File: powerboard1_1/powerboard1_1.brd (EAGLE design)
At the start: 149.9 x 86.4 mm, 103 parts, among them Q1 IPP80P03P4L04AKSA1, U1 UWQ-12/20-T48NBS-C, U2 UWE-5/20-Q48NB-C, U3 UWE-3.3/30-Q48NB-C

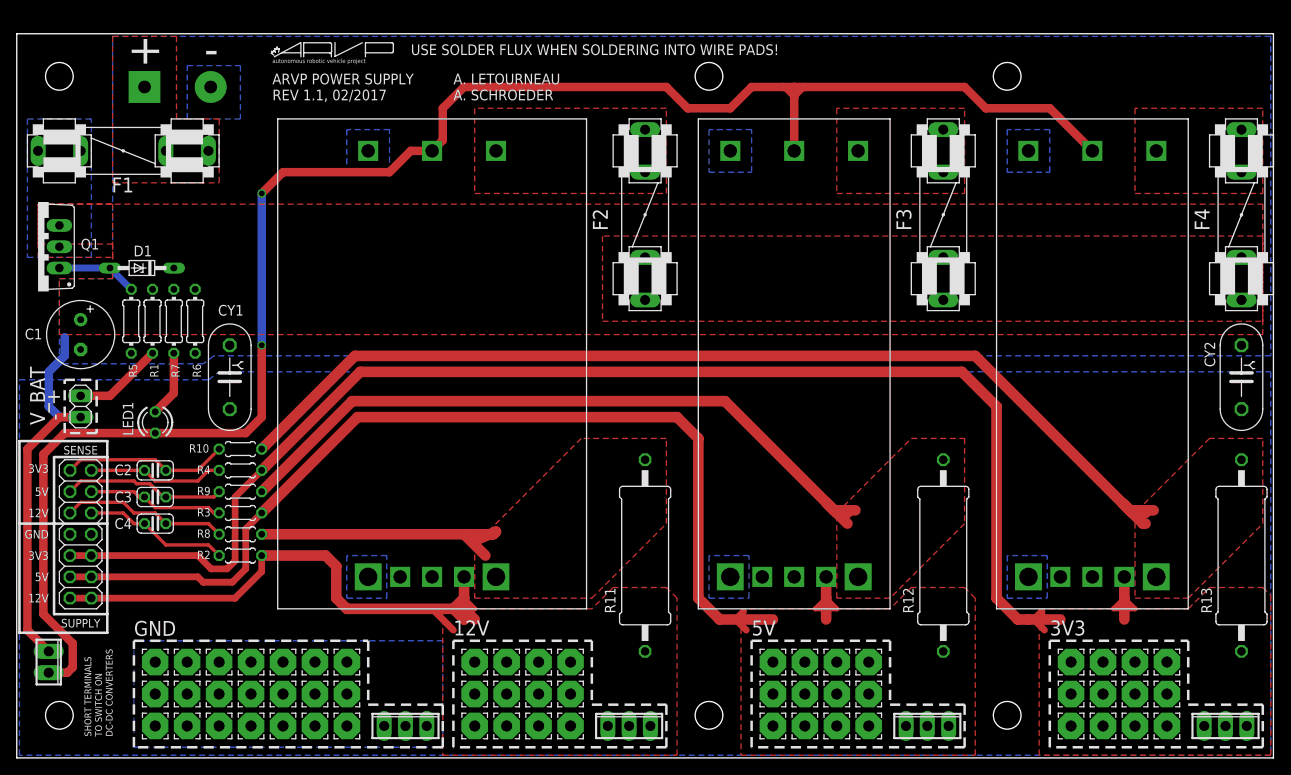
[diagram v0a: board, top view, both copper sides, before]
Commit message: Modified more traces and polygons; Fixed power board library
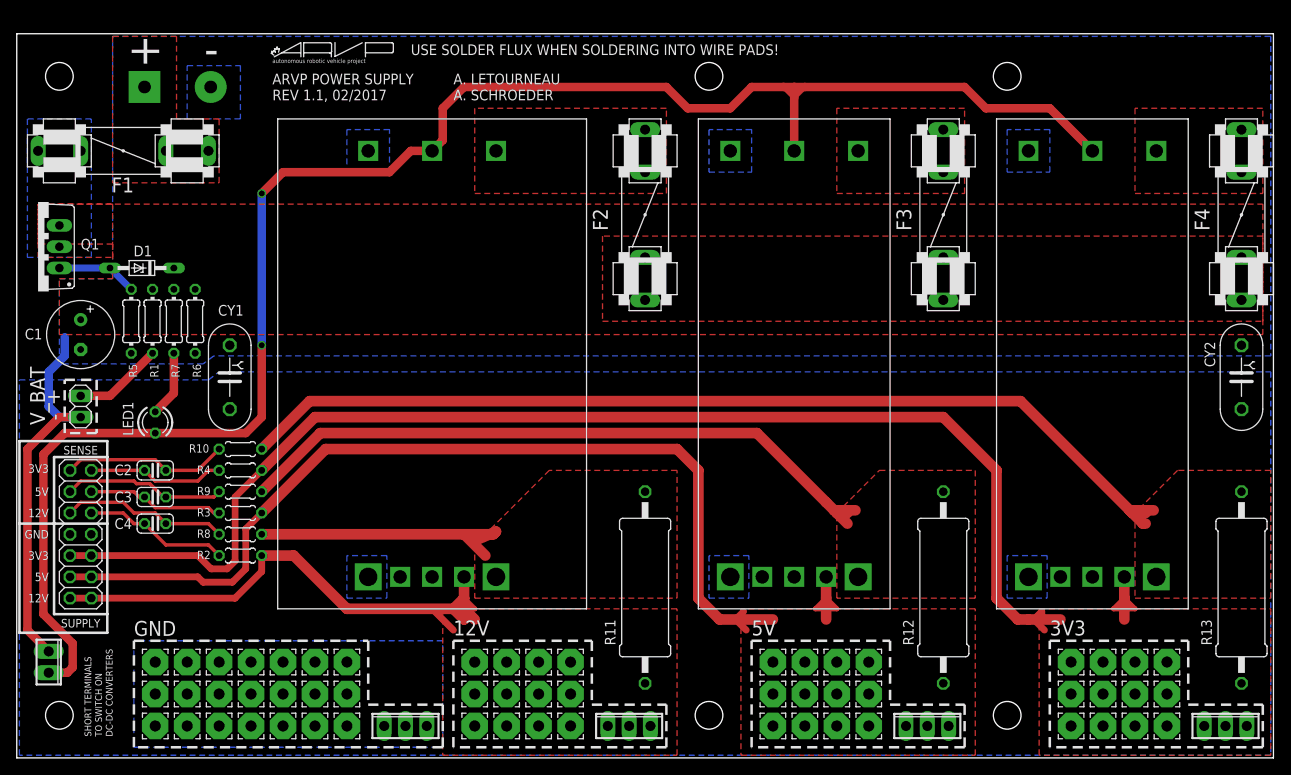
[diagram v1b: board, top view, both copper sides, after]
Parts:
- U4: value UWQ-12/20-T48NBS-C -> UWQ-12/20-T48NTB-C
- moved R11 3.81 mm to (104.1, 11.4)
- moved R12 3.81 mm to (139.7, 11.4)
- moved R13 3.81 mm to (175.3, 11.4)
- renumbered U1 to U4
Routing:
- net 3V3-SENSE: track 174.7 -> 165.7 mm
- net 3V3+SENSE: track 125.4 -> 118.3 mm
- net 5V+SENSE: track 87.3 -> 81.0 mm
- net 5V-SENSE: track 131.2 -> 125.8 mm
- net 12V-SENSE: track 73.5 -> 71.2 mm

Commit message: Replaced output rail terminals with filtering capacitors; Modified LED circuit; Modified traces and polygons
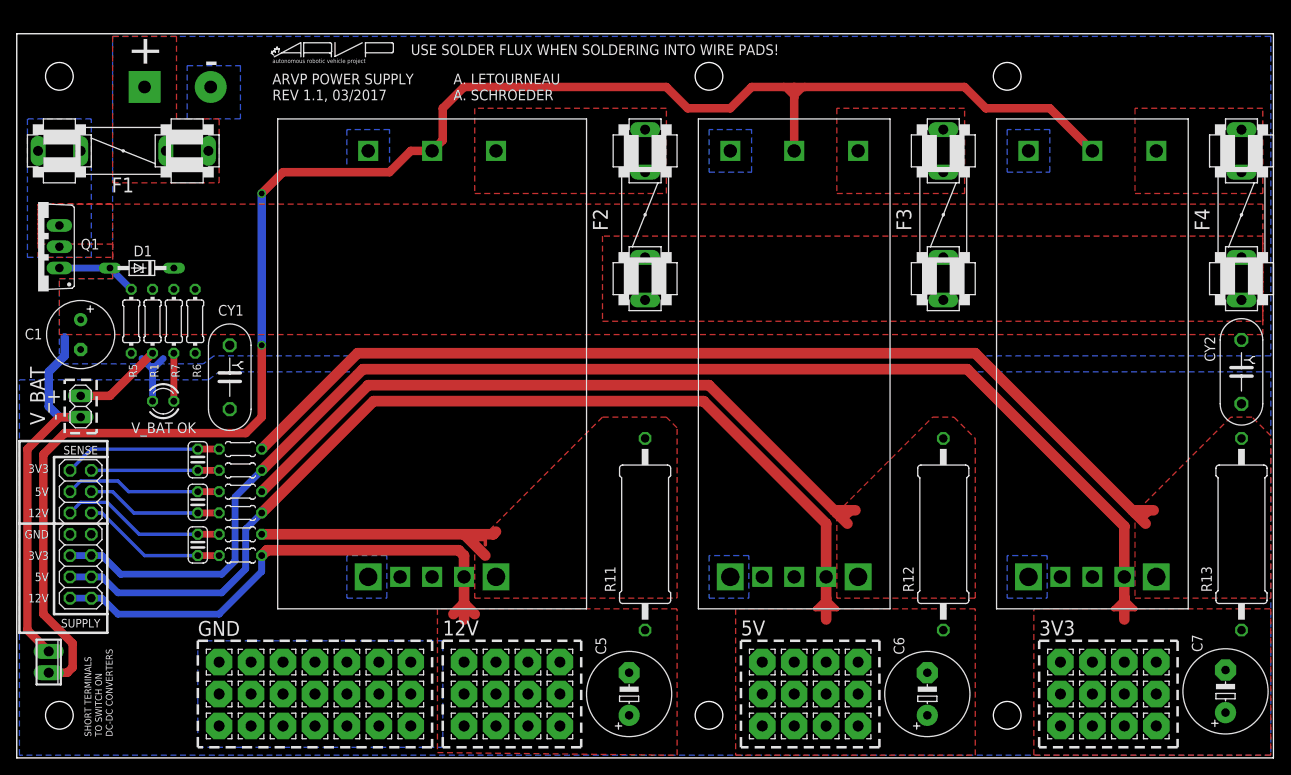
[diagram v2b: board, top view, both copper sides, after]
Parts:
- removed X2, X3, X4, X5: (no value), con-phoenix-254:3POL254
- added C5, C6, C7: (no value), rcl:E5-10,5
- moved PAD12 7.62 mm to (53.3, -1.27)
- moved PAD13 7.62 mm to (76.2, -5.08)
- moved PAD14 7.62 mm to (72.4, -5.08)
- moved PAD19 7.62 mm to (53.3, 2.54)
- moved PAD20 7.62 mm to (76.2, -1.27)
- moved PAD21 7.62 mm to (72.4, -1.27)
- moved PAD5 7.62 mm to (72.4, 2.54)
- moved PAD6 7.62 mm to (76.2, 2.54)
- moved PAD7 7.62 mm to (53.3, -5.08)
- moved PAD1 7.62 mm to (57.1, 2.54)
- moved PAD10 7.62 mm to (64.8, -1.27)
- moved PAD11 7.62 mm to (68.6, -1.27)
- moved PAD15 7.62 mm to (68.6, -5.08)
- moved PAD16 7.62 mm to (64.8, -5.08)
- moved PAD17 7.62 mm to (61.0, -5.08)
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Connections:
- net 12V-SENSE: now also C5.+; no longer X2.1, X2.2, X2.3
- net 3V3-SENSE: now also C7.+; no longer X5.1, X5.2, X5.3
- net 5V-SENSE: now also C6.+; no longer X4.1, X4.2, X4.3
- net GND: now also C5.-, C6.-, C7.-; no longer X3.1, X3.2, X3.3
- net ON/OFF: no longer LED1.K
- net V-: now also LED1.K
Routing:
- net V-: track 46.5 -> 54.2 mm
- net 12V-SENSE: track 71.2 -> 63.5 mm
- net 5V+SENSE: track 81.0 -> 85.8 mm
- net 3V3+SENSE: track 118.3 -> 122.4 mm
- net N$1: track 7.91 -> 5.71 mm
- net J8: track 19.9 -> 18.8 mm
- net J7: track 16.3 -> 15.2 mm
- net 5V-SENSE: track 125.8 -> 126.8 mm
- net J6: track 19.4 -> 18.8 mm
- net 3V3-SENSE: track 165.7 -> 166.2 mm
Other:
- board text added: "REV 1.1, 03/2017"
- board text added: "V_BAT OK"
- board text removed: "REV 1.1, 02/2017"

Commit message: Added open collector control circuit; Added input filtering capacitors
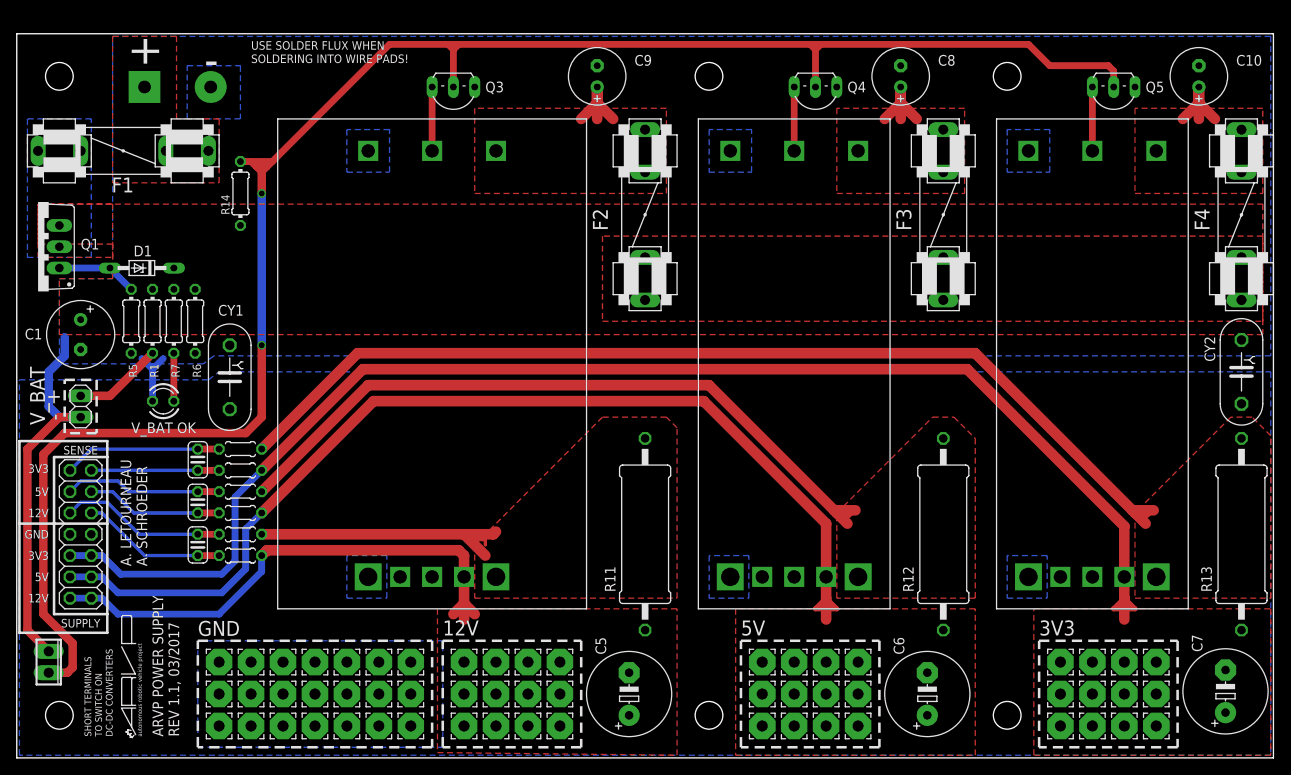
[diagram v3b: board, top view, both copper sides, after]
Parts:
- added C10, C8, C9: (no value), resistor:E2,5-7
- added Q3, Q4, Q5: 2N4401TFR, New Power Board Library:TO92-EBC
- added R14: 4.7k, resistor:0204/7
- moved U$3 81.8 mm to (44.1, -6.35), turned to 90 degrees
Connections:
- removed net N$6: F3.2A, F3.2B, U2.+VIN
- removed net N$7: F4.2A, F4.2B, U3.+VIN
- new net N$10: Q4.C, U2.RC
- new net N$11: Q5.C, U3.RC
- new net N$13: C10.+, F4.2A, F4.2B, U3.+VIN
- new net N$8: Q3.C, U4.RC
- new net N$9: C8.+, F3.2A, F3.2B, U2.+VIN
- net N$5: now also C9.+
- net ON/OFF: now also Q3.B, Q4.B, Q5.B, R14.2; no longer U2.RC, U3.RC, U4.RC
- net V+: now also R14.1
- net V-: now also C10.-, C8.-, C9.-, Q3.E, Q4.E, Q5.E
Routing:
- net ON/OFF: track 207.5 -> 222.3 mm
- net N$9: track 0.00 -> 13.0 mm
- net N$5: track 0.00 -> 13.0 mm
- net N$13: track 0.00 -> 13.0 mm
- net N$8: track 0.00 -> 7.62 mm
- net N$11: track 0.00 -> 7.62 mm
- net N$10: track 0.00 -> 7.62 mm
- added copper zone on layer 1, net N$13
- added copper zone on layer 1, net N$9
- removed copper zone on layer 1, net N$6
- removed copper zone on layer 1, net N$7
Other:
- board text added: "SOLDERING INTO WIRE PADS!"
- board text added: "USE SOLDER FLUX WHEN"
- board text removed: "USE SOLDER FLUX WHEN SOLDERING INTO WIRE PADS!"

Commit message: Modifed some routing, text/graphics positions
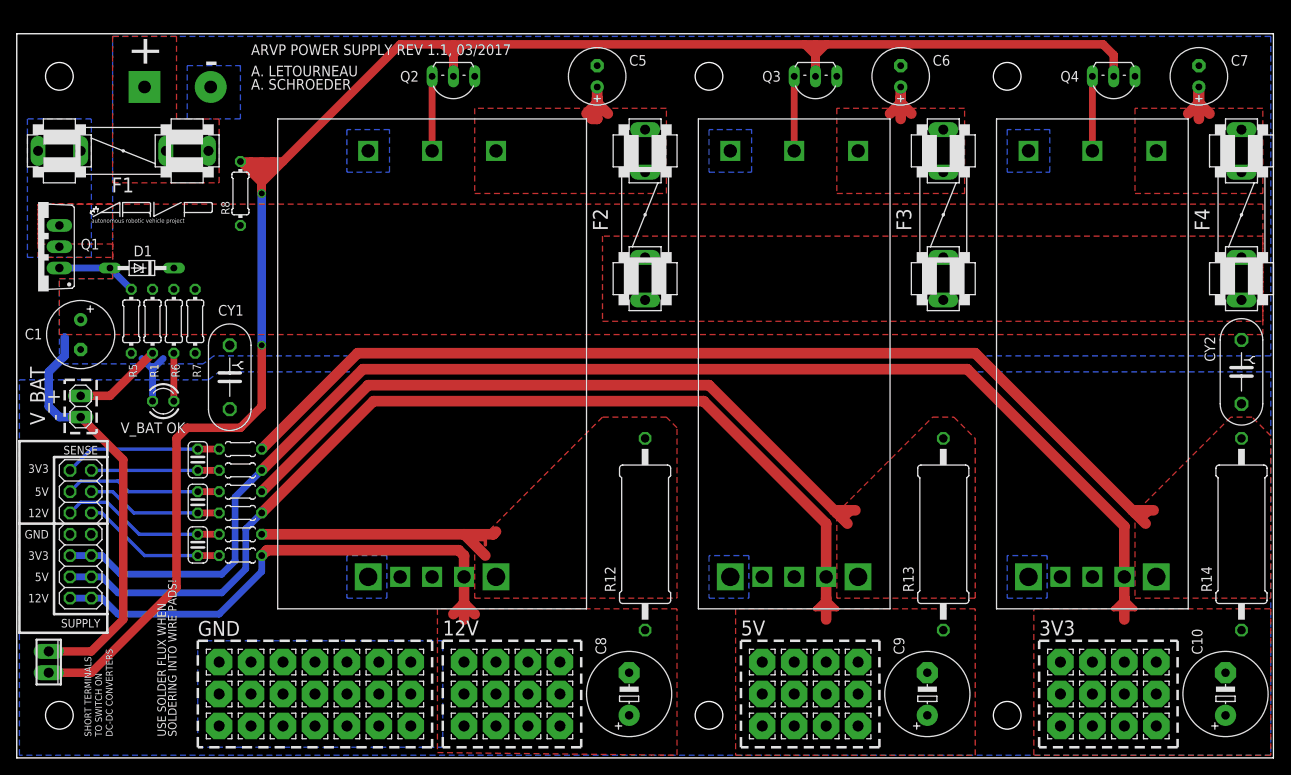
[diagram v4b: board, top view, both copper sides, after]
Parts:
- removed Q5: 2N4401TFR, New Power Board Library:TO92-EBC
- added Q2: 2N4401TFR, New Power Board Library:TO92-EBC
- C10, C8, C9: device resistor:E2,5-7 -> rcl:E5-10,5
- C5, C6, C7: device rcl:E5-10,5 -> rcl:E2,5-7
- R11: value 0.004 -> 10; device rcl:0617/22 -> rcl:0204/5
- R14: value 4.7k -> 0.004; device resistor:0204/7 -> rcl:0617/22
- R6: value 4.7k -> 36k
- R7: value 36k -> 4.7k
- R8: value 10 -> 4.7k; device rcl:0204/5 -> resistor:0204/7
- moved R14 126.1 mm to (175.3, 17.8), turned to 270 degrees
- moved C9 83.5 mm to (137.8, -1.27)
- moved C8 80.5 mm to (102.2, -1.27)
- moved C5 73.8 mm to (98.4, 72.4)
- moved C10 73.7 mm to (173.4, -1.27)
- moved C6 73.7 mm to (134.6, 72.4)
- moved C7 73.4 mm to (170.2, 72.4)
- moved U$3 61.6 mm to (38.1, 54.9), turned to 0 degrees
- moved R11 49.3 mm to (55.9, 27.9), turned to 0 degrees
- moved Q3 43.2 mm to (124.5, 71.1)
- moved R8 40.6 mm to (55.9, 58.4), turned to 90 degrees
- moved Q4 35.6 mm to (160.0, 71.1)
- moved R13 35.6 mm to (139.7, 17.8)
- moved R12 35.6 mm to (104.1, 17.8)
- moved R10 5.08 mm to (55.9, 22.9)
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- renumbered U4 to U1
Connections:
- net 12V+SENSE: now also R12.1, R9.2; no longer R11.1, R8.2
- net 12V-SENSE: now also C8.+, R12.2; no longer C5.+, R11.2
- net 3V3+SENSE: now also R11.2, R14.1; no longer R10.2, R13.1
- net 3V3-SENSE: now also C10.+, R14.2; no longer C7.+, R13.2
- net 5V+SENSE: now also R10.2, R13.1; no longer R12.1, R9.2
- net 5V-SENSE: now also C9.+, R13.2; no longer C6.+, R12.2
- net GND: now also C10.-, C8.-, C9.-; no longer C5.-, C6.-, C7.-
- net J4: now also R9.1; no longer R8.1
- net J6: now also R10.1; no longer R9.1
- net J8: now also R11.1; no longer R10.1
- net N$1: now also R6.1; no longer R7.1
- net N$10: now also Q3.C; no longer Q4.C
- net N$11: now also Q4.C; no longer Q5.C
- net N$13: now also C7.+; no longer C10.+
- net N$5: now also C5.+; no longer C9.+
- net N$8: now also Q2.C; no longer Q3.C
- net N$9: now also C6.+; no longer C8.+
- net ON/OFF: now also Q2.B, R8.2; no longer Q5.B, R14.2
- net V+: now also R6.2, R7.1, R8.1; no longer R14.1, R6.1, R7.2
- net V-: now also C5.-, C6.-, C7.-, Q2.E, R7.2; no longer C10.-, C8.-, C9.-, Q5.E, R6.2
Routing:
- net N$9: track 13.0 -> 7.40 mm
- net N$5: track 13.0 -> 9.31 mm
- net N$13: track 13.0 -> 9.31 mm
- net V-: track 54.2 -> 57.8 mm
- net ON/OFF: track 222.3 -> 225.6 mm
- net N$8: track 7.62 -> 8.89 mm
- net N$11: track 7.62 -> 8.89 mm
- net N$10: track 7.62 -> 8.89 mm
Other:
- board text added: "ARVP POWER SUPPLY REV 1.1, 03/2017"
- board text removed: "ARVP POWER SUPPLY"
- board text removed: "REV 1.1, 03/2017"
